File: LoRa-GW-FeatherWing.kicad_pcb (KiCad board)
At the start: 4 copper layers, 51.3 x 23.4 mm, 116 parts, among them J1 Conn_Coaxial, J2 Conn_Coaxial, U1 SX1303IMLTRT, U2 SX1250, U3 SX1250, U4 TPS7A91, U5 JT255BI0032.000000, U6 TLV62568DRL, U7 SKY66420-11, U8 EVA-8M

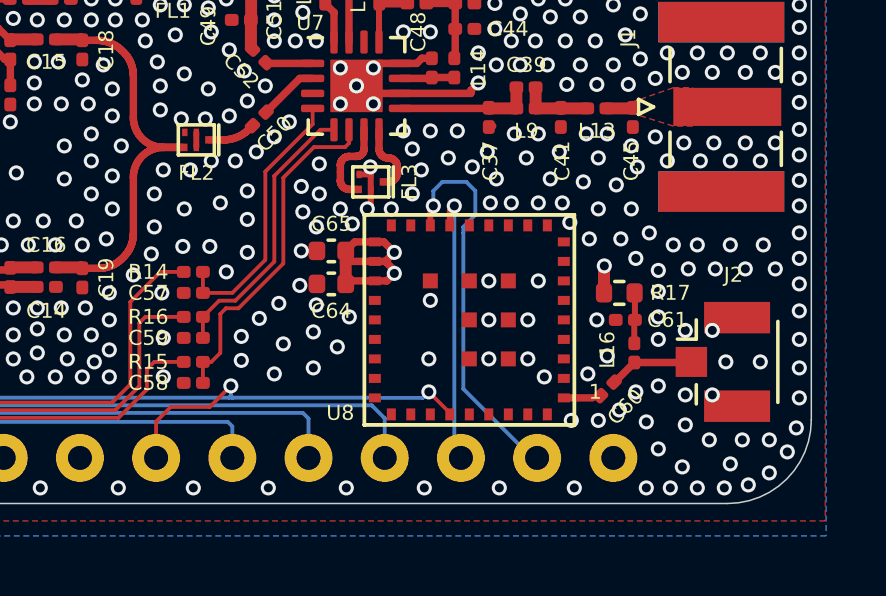
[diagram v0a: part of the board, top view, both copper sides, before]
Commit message: Fixing GPS TX RX pin flipped issue
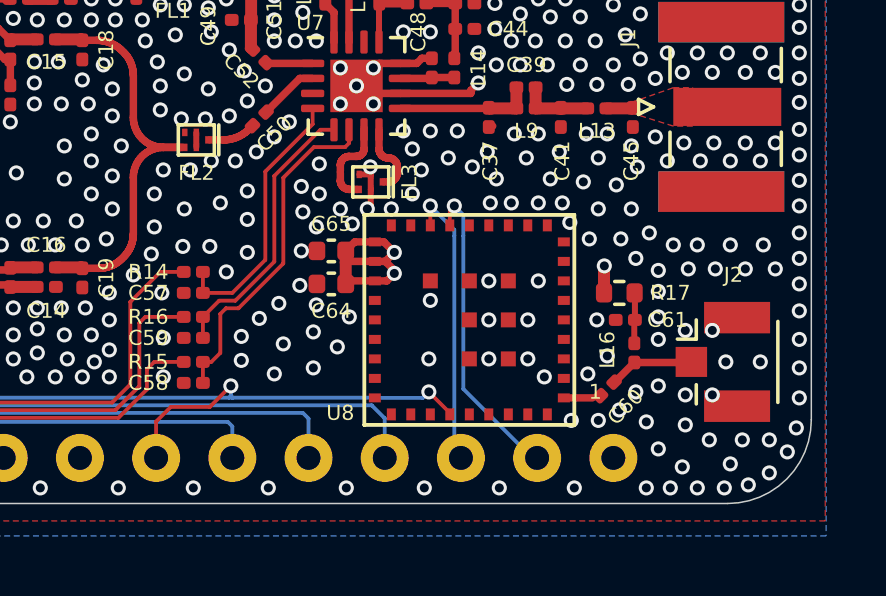
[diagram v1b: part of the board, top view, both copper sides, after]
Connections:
- U8 pad 15: GPS_TX -> GPS_RX
- U8 pad 16: GPS_RX -> GPS_TX
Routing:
- net GPS_RX: track 13.3 -> 10.6 mm

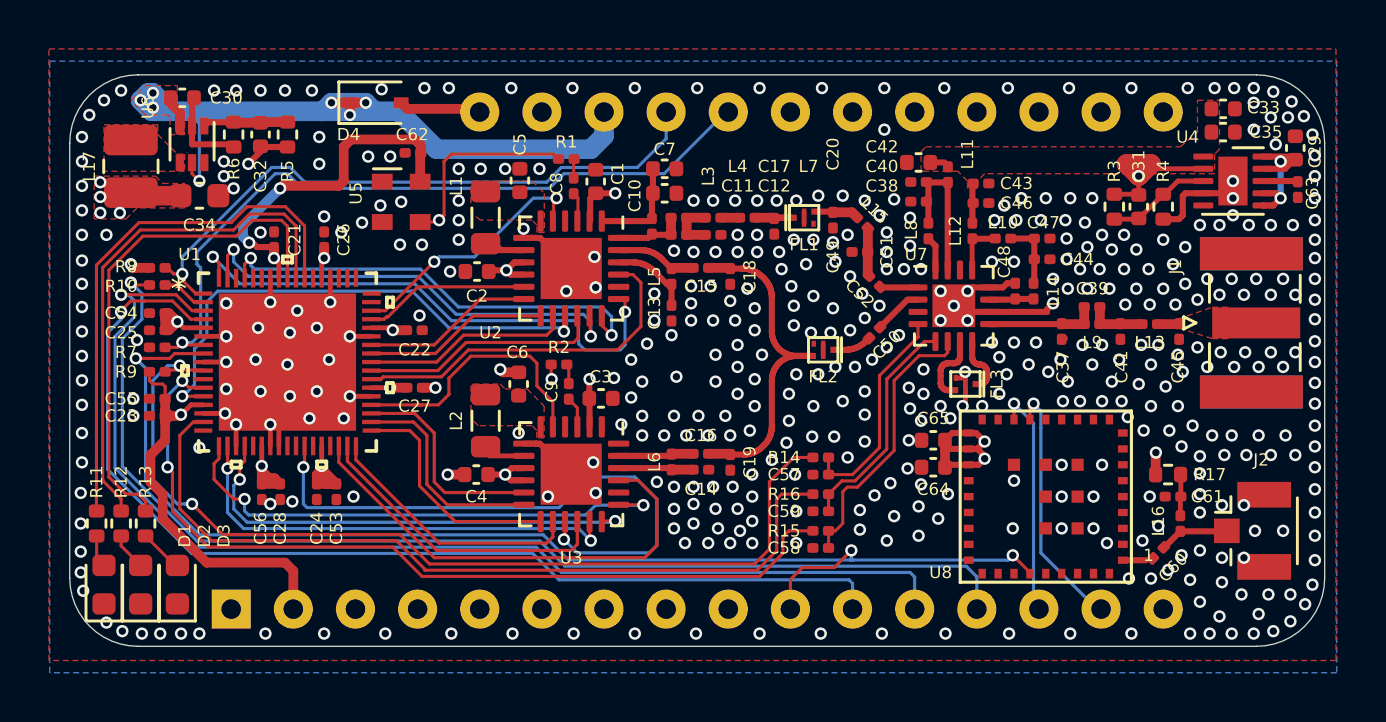
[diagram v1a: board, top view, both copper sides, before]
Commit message: Adding SX1261 for LBT
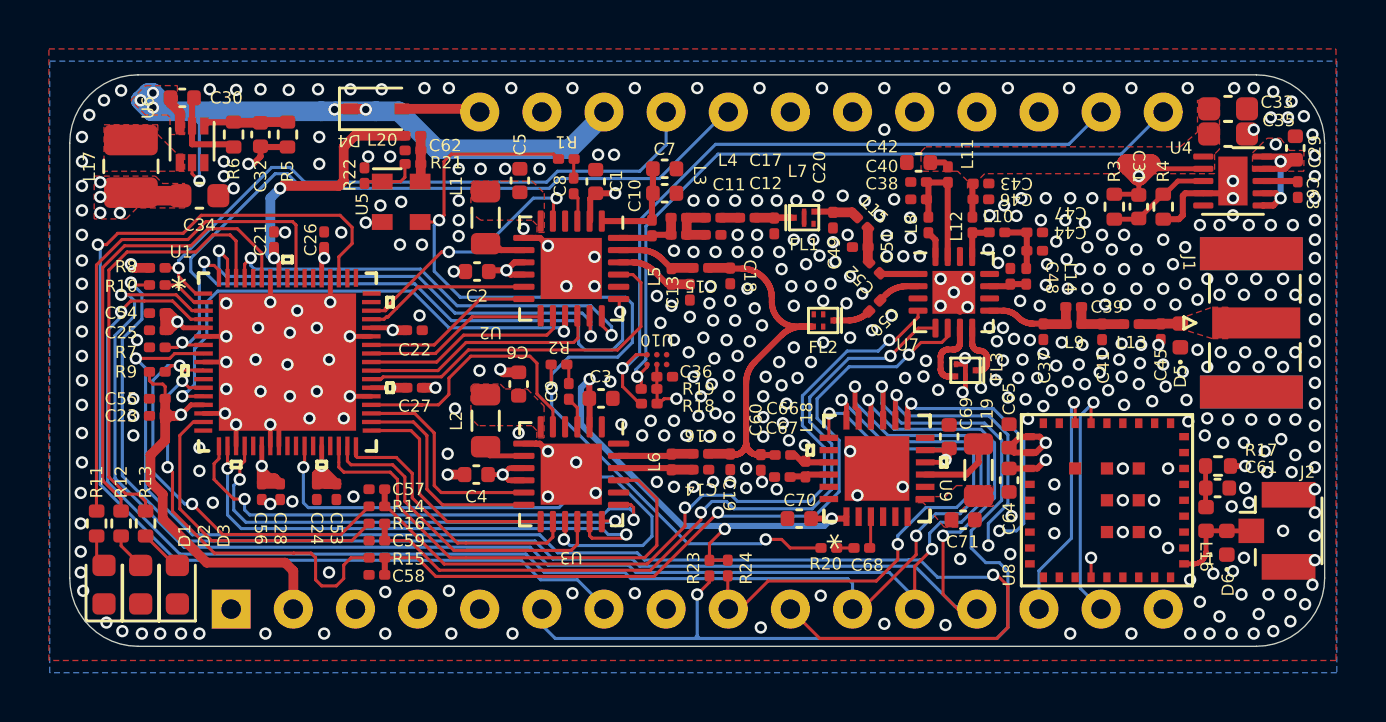
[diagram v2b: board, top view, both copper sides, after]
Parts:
- added C36: 3pF, Capacitor_SMD:C_0201_0603Metric, F.Cu at (127.2, 68.2)
- added C66: 3.6pF, Capacitor_SMD:C_0201_0603Metric, F.Cu at (132.1, 71.4)
- added C67: 3.6pF, Capacitor_SMD:C_0201_0603Metric, F.Cu at (132.0, 72.3)
- added C68: 10pF, Capacitor_SMD:C_0201_0603Metric, F.Cu at (135.3, 75.2)
- added C69: 1uF, Capacitor_SMD:C_0402_1005Metric, F.Cu at (138.8, 70.7)
- added C70: 1uF, Capacitor_SMD:C_0402_1005Metric, F.Cu at (132.7, 74.0)
- added C71: 470nF, Capacitor_SMD:C_0402_1005Metric, F.Cu at (139.4, 74.0)
- added D5: D_TVS, Diode_SMD:D_0402_1005Metric, F.Cu at (148.3, 66.5)
- added D6: D_TVS, Diode_SMD:D_0402_1005Metric, F.Cu at (150.2, 75.0)
- added L18: 18nH, Inductor_SMD:L_0201_0603Metric, F.Cu at (133.0, 72.0)
- added L19: MLZ2012N150LT000, Inductor_SMD:L_0805_2012Metric, F.Cu at (140.1, 72.0)
- added L20: FB, Inductor_SMD:L_0201_0603Metric, F.Cu at (116.9, 58.4)
- added R18: 100K, Resistor_SMD:R_0201_0603Metric, F.Cu at (126.6, 69.3)
- added R19: 100K, Resistor_SMD:R_0201_0603Metric, F.Cu at (126.6, 68.7)
- added R20: 220R, Resistor_SMD:R_0201_0603Metric, F.Cu at (133.9, 75.2)
- added R21: 220R, Resistor_SMD:R_0201_0603Metric, F.Cu at (116.9, 59.5)
- added R22: 220R, Resistor_SMD:R_0201_0603Metric, F.Cu at (115.0, 60.0)
- added R23: 220R, Resistor_SMD:R_0201_0603Metric, F.Cu at (129.1, 76.0)
- added R24: 220R, Resistor_SMD:R_0201_0603Metric, F.Cu at (129.8, 76.0)
- added U10: TMP117AIYBGR, SX1302:TMP117AIYBGR, F.Cu at (126.9, 67.5)
- added U9: SX1262IMLTRT, SX1302:SX1262IMLTRT, F.Cu at (135.9, 72.0)
- C33, C35: footprint Capacitor_SMD:C_0402_1005Metric -> Capacitor_SMD:C_0603_1608Metric
- C60: value 0R -> DNP
- C61: footprint Capacitor_SMD:C_0201_0603Metric -> Capacitor_SMD:C_0402_1005Metric
- L16: footprint Inductor_SMD:L_0201_0603Metric -> Inductor_SMD:L_0402_1005Metric
- moved R14 18.3 mm to (115.5, 73.5)
- moved C59 18.2 mm to (115.5, 74.9)
- moved R16 18.2 mm to (115.5, 74.2)
- moved C58 18.2 mm to (115.5, 76.3)
- moved R15 18.2 mm to (115.5, 75.6)
- moved C57 18.2 mm to (115.5, 72.8)
- moved C60 16.7 mm to (131.2, 71.7), turned to -90 degrees
- moved C64 3.14 mm to (141.3, 72.4), turned to -90 degrees
- moved C65 3.11 mm to (141.3, 70.6), turned to 90 degrees
- moved U8 2.50 mm to (145.3, 73.2)
- moved R17 2.07 mm to (149.8, 71.8), turned to 180 degrees
- moved C61 1.85 mm to (149.8, 72.8), turned to 180 degrees
- moved FL2 1.20 mm to (133.7, 65.9)
- moved C13 1.14 mm to (128.2, 64.7)
- moved C50 1.09 mm to (135.8, 65.3)
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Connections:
- A1 pad 17: Net-(A1-Pad17) -> SDA
- A1 pad 18: Net-(A1-Pad18) -> SCL
- A1 pad 6: Net-(A1-Pad6) -> SX1262_RESET
- A1 pad 7: Net-(A1-Pad7) -> SX1261_DIO1
- A1 pad 8: Net-(A1-Pad8) -> SX1261_BUSY
- A1 pad 9: Net-(A1-Pad9) -> SX1261_CSN
- C2 pad 1: VDD_RF -> +3V3
- C4 pad 1: VDD_RF -> +3V3
- C60 pad 1: Net-(C60-Pad1) -> Net-(C15-Pad1)
- C60 pad 2: Net-(C60-Pad2) -> GND
- C62 pad 1: +3V3 -> Net-(C62-Pad1)
- J2 pad 1: Net-(C60-Pad1) -> Net-(D6-Pad2)
- L16 pad 2: Net-(C60-Pad1) -> Net-(D6-Pad2)
- U1 pad 54: Net-(U1-Pad54) -> SX1261_DIO1
- U1 pad 58: Net-(R11-Pad2) -> Net-(U1-Pad58)
- U1 pad 59: Net-(R12-Pad2) -> Net-(R11-Pad2)
- U1 pad 60: Net-(R13-Pad2) -> Net-(U1-Pad60)
- U1 pad 63: Net-(U1-Pad63) -> Net-(R12-Pad2)
- U1 pad 66: Net-(U1-Pad66) -> Net-(R13-Pad2)
- U2 pad 10: VDD_RF -> +3V3
- U2 pad 9: VDD_RF -> +3V3
- U3 pad 10: VDD_RF -> +3V3
- U3 pad 9: VDD_RF -> +3V3
- U5 pad 1: GND -> Net-(R21-Pad1)
- U5 pad 4: +3V3 -> Net-(C62-Pad1)
- U8 pad 1: Net-(C60-Pad2) -> Net-(D6-Pad2)
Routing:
- net SX1261_DIO1: track 0.00 -> 75.4 mm, vias 0 -> 3
- net SX1262_RESET: track 0.00 -> 40.1 mm, vias 0 -> 2
- net SDA: track 0.00 -> 30.7 mm, vias 0 -> 1
- net SCL: track 0.00 -> 30.1 mm, vias 0 -> 1
- net SX1261_BUSY: track 0.00 -> 26.6 mm, vias 0 -> 2
- net SX1261_CSN: track 0.00 -> 23.1 mm, vias 0 -> 2
- net CSD: track 8.94 -> 32.0 mm, vias 0 -> 2
- net TCXO_32Mhz: track 17.8 -> 40.5 mm, vias 2 -> 3
- net PA_ON: track 9.33 -> 31.7 mm, vias 0 -> 2
- net SX1303_CSD: track 39.1 -> 17.3 mm
- net SX1303_PA_ON: track 33.7 -> 12.8 mm
- net TXRX: track 11.5 -> 32.1 mm, vias 0 -> 2
- net VDD_RF: track 57.6 -> 76.4 mm, vias 5 -> 7
- net SX1303_TXRX: track 35.1 -> 17.4 mm
- net HOST_SCK: track 43.8 -> 60.9 mm, vias 1 -> 3
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- added copper zone on F.Cu, net Net-(C71-Pad1)
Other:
- board text added: "SX1303 LoRa Gateway With LBT FeatherWing Design By Will Whang 2021/03/12"
- board text removed: "SX1303 LoRa Gateway For Feather Boards Design By Will Whang 2020/12/20"
